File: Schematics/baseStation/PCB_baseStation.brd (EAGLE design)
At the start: 53 x 60 mm, 39 parts, among them U1 ATMEGA328P, U2 MCP1824ST-3302E/DB, Y2 16MHz

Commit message: Base Station PCB improvements
Base_SP 1.1
moved prop plug and ISP closer in
added two resistors to limit voltage from arduino to xbee pin 9(SLP)
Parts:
- added R10: 3.3k, SparkFun-Resistors:0603-RES
- added R9: 1.8k, SparkFun-Resistors:0603-RES
- moved R2 6.48 mm to (17.8, 35.6)
- moved R1 6.48 mm to (17.8, 41.9)
- moved R4 6.48 mm to (17.8, 47.0)
- moved C1 6.35 mm to (29.2, 47.0)
- moved U2 6.35 mm to (22.9, 52.1)
- moved R6 5.08 mm to (27.9, 34.3)
- moved U$1 5.08 mm to (22.9, 30.5)
- moved R3 4.02 mm to (27.9, 24.1)
- moved GND13 3.81 mm to (6.35, 30.5)
- moved RST2 3.81 mm to (6.35, 33.0)
- moved RX1 3.81 mm to (6.35, 35.6)
- moved TX1 3.81 mm to (6.35, 38.1)
- moved 1 3.81 mm to (44.5, 49.5)
- moved 2 3.81 mm to (47.0, 49.5)
- moved 3 3.81 mm to (44.5, 47.0)
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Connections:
- new net N$6: R10.1, R9.2, U$1.9
- new net PD4: R9.1, U1.2
- net GND: now also R10.2
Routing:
- net PD4: track 0.00 -> 27.5 mm, vias 0 -> 2
- net N$6: track 0.00 -> 24.7 mm
- net N$15: track 22.6 -> 12.2 mm, vias 4 -> 0
- net N$19: track 73.3 -> 64.8 mm, vias 1 -> 2
- net DOUT: track 47.6 -> 41.2 mm
- net N$13: track 36.9 -> 42.1 mm, vias 1 -> 2
- net DIN: track 39.7 -> 35.5 mm
- net 4: track 32.5 -> 29.6 mm, vias 0 -> 1
- net N$4: track 3.94 -> 6.08 mm
- net N$10: track 43.1 -> 44.9 mm
- net N$20: track 66.6 -> 65.1 mm
- net 3: track 32.0 -> 30.6 mm, vias 1 -> 0
- net N$14: track 9.40 -> 10.7 mm
- net N$9: track 21.8 -> 20.8 mm
- net N$3: track 16.1 -> 15.1 mm
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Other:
- board text added: "BASE_SP 1.1"
- board text removed: "BASE_SP 1.0"

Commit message: Base Station PCB Improvements
Base_SP 1.3
fixed SIM900 pins that go to Arduino
changed xbee pin that goes to Arduino
created table of base Arduino pins and where they go to
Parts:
- added SM_5V, SM_PWR: M01PTH, SparkFun-Connectors:1X01
- moved R6 19.1 mm to (12.7, 22.9)
- moved PWR 18.2 mm to (18.4, 2.54)
- moved R10 16.6 mm to (17.8, 31.8), turned to 180 degrees
- moved R8 14.0 mm to (36.8, 35.6)
- moved C2 10.5 mm to (16.5, 7.62), turned to 90 degrees
- moved R9 7.41 mm to (17.8, 35.6)
- moved R3 6.84 mm to (30.5, 17.8)
- moved R7 6.48 mm to (12.7, 17.8), turned to 90 degrees
- moved R5 3.81 mm to (49.5, 35.6)
- moved R2 3.81 mm to (17.8, 39.4)
- moved SOLAR 2.54 mm to (25.4, 4.45)
- moved R1 1.27 mm to (17.8, 43.2)
- renumbered GND to SM_GND, RST to SM_RST, RX to SM_RX, TX to SM_TX
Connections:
- new net PB0: SM_TX.1, U1.12
- new net PD2: SM_PWR.1, U1.32
- new net PD3: SM_RST.1, U1.1
- new net PD7: SM_RX.1, U1.11
- net N$19: no longer SM_TX.1
- net N$20: no longer SM_RX.1
- net RST: no longer SM_RST.1
- net VCC: now also SM_5V.1; no longer 5V.1
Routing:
- net VCC: track 144.3 -> 250.7 mm, vias 2 -> 3
- net RST: track 102.7 -> 179.4 mm, vias 2 -> 5
- net N$21: track 0.00 -> 65.1 mm, vias 0 -> 2
- net N$19: track 64.8 -> 122.1 mm, vias 2 -> 3
- net N$10: track 44.9 -> 97.5 mm, vias 1 -> 2
- net PD3: track 0.00 -> 46.3 mm, vias 0 -> 1
- net PD7: track 0.00 -> 44.3 mm, vias 0 -> 1
- net PD2: track 0.00 -> 42.5 mm, vias 0 -> 1
- net PB0: track 0.00 -> 41.6 mm, vias 0 -> 1
- net DOUT: track 41.2 -> 82.6 mm, vias 2 -> 4
- net DIN: track 35.5 -> 73.6 mm, vias 2 -> 4
- net 4: track 29.6 -> 65.2 mm, vias 1 -> 0
- net 1: track 32.8 -> 61.8 mm
- net PD4: track 27.5 -> 55.5 mm, vias 2 -> 0
- net 3: track 30.6 -> 55.2 mm, vias 0 -> 1
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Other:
- board text added: "BASE_SP 1.2"
- board text added: "BASE_SP 1.3"
- board text removed: "BASE_SP 1.1"

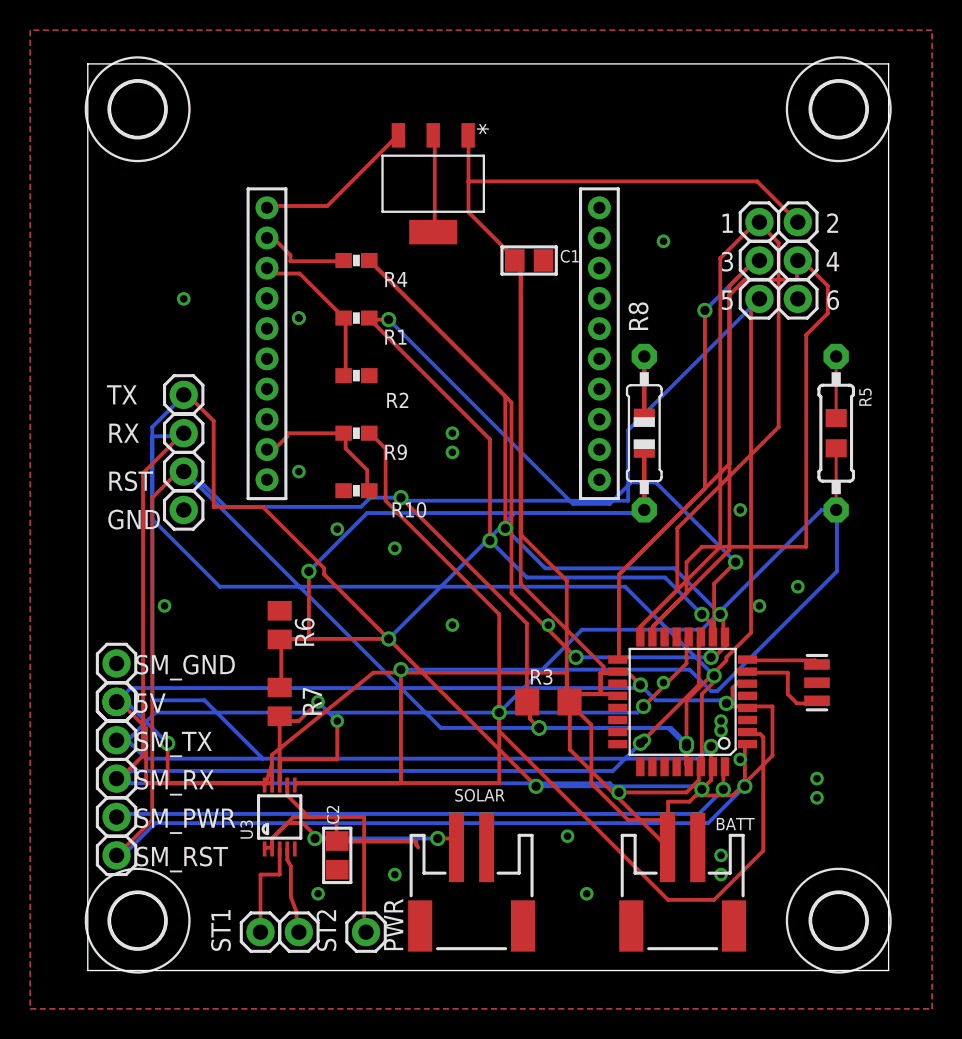
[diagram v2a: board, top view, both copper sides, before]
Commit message: PCB Base Station Improvements
Base_SP 1.4
fixed issues that were occurring with code
fixed SIM900 pins that go to Arduino
changed xbee pin that goes to Arduino
created table of base Arduino pins and where they go to
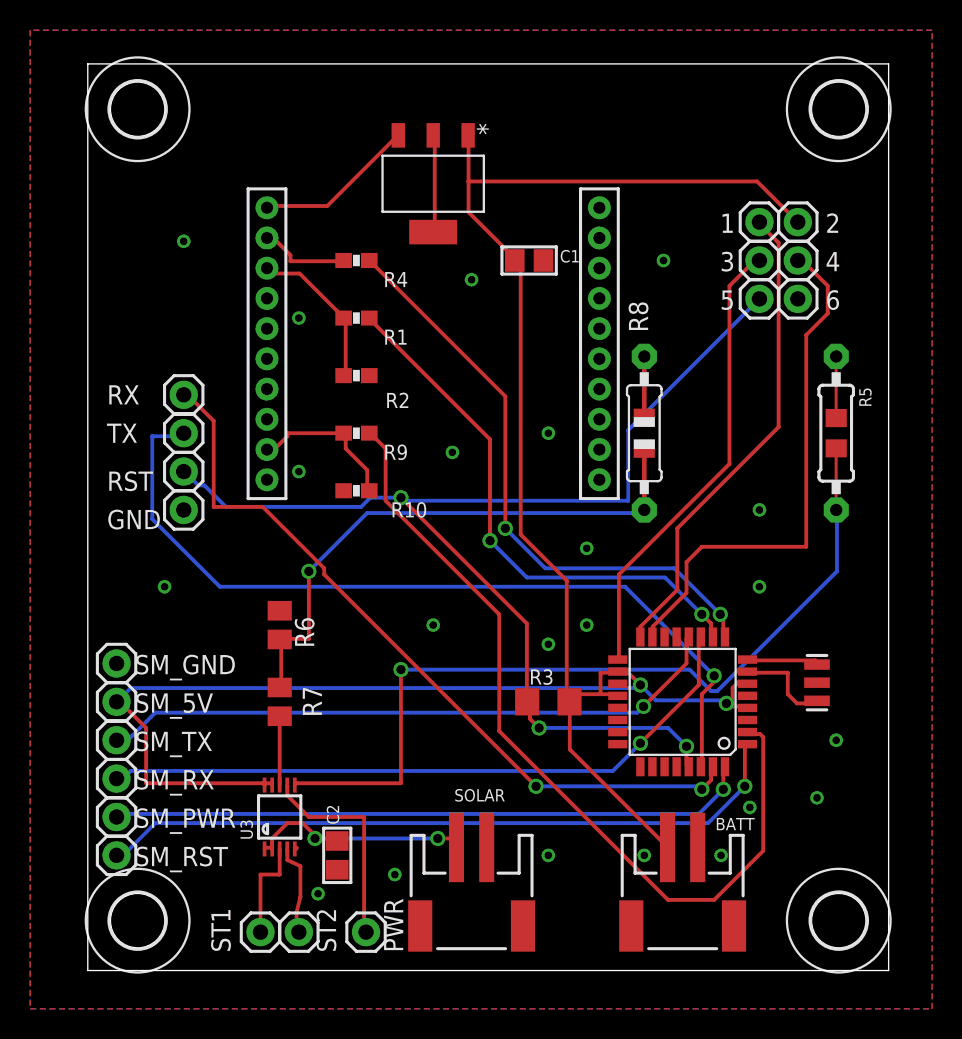
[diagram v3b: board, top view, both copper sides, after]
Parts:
- removed 5V: M01PTH, SparkFun-Connectors:1X01
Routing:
- net VCC: track 250.7 -> 144.0 mm, vias 3 -> 2
- net RST: track 179.4 -> 78.4 mm, vias 5 -> 3
- net N$19: track 122.1 -> 50.6 mm, vias 3 -> 2
- net N$21: track 65.1 -> 0.00 mm, vias 2 -> 0
- net N$10: track 97.5 -> 51.4 mm, vias 2 -> 1
- net DOUT: track 82.6 -> 39.7 mm, vias 4 -> 2
- net DIN: track 73.6 -> 35.9 mm, vias 4 -> 2
- net 4: track 65.2 -> 34.9 mm
- net 1: track 61.8 -> 31.8 mm
- net N$13: track 61.2 -> 33.5 mm, vias 2 -> 1
- net 3: track 55.2 -> 30.6 mm, vias 1 -> 0
- net N$15: track 17.8 -> 4.56 mm, vias 2 -> 0
- net N$9: track 28.8 -> 16.6 mm
- net GND: track 0.00 -> 0.40 mm, vias 27 -> 22
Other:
- board text added: "BASE_SP 1.4"
- board text removed: "BASE_SP 1.2"
- board text removed: "BASE_SP 1.3"

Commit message: Base Station PCB Improvements
Base_SP 1.5
- Fix: connected Regulator for XBee to GND
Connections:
- removed net N$12: U2.2, U2.4
- net GND: now also U2.2, U2.4
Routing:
- net N$12: track 6.54 -> 0.00 mm
- net GND: track 0.40 -> 6.94 mm
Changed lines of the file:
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@@
 <wire x1="48.1584" y1="20.32" x2="48.26" y2="20.25" width="0.254" layer="1"/>
-</signal>
-<signal name="N$12">
-<contactref element="U2" pad="4"/>
-<contactref element="U2" pad="2"/>
-<wire x1="22.9616" y1="48.9712" x2="22.9616" y2="55.2704" width="0.254" layer="1"/>
-<wire x1="22.9616" y1="55.2704" x2="22.86" y2="55.2704" width="0.254" layer="1"/>
-<wire x1="22.9616" y1="48.9712" x2="22.86" y2="48.8696" width="0.254" layer="1"/>
 </signal>
 <signal name="N$14">
@@
 <via x="38.1" y="46.99" extent="1-16" drill="0.5"/>
 <via x="44.45" y="30.48" extent="1-16" drill="0.5"/>
+<contactref element="U2" pad="4"/>
+<contactref element="U2" pad="2"/>
+<wire x1="22.9616" y1="48.9712" x2="22.9616" y2="55.2704" width="0.254" layer="1"/>
+<wire x1="22.9616" y1="55.2704" x2="22.86" y2="55.2704" width="0.254" layer="1"/>
+<wire x1="22.9616" y1="48.9712" x2="22.86" y2="48.8696" width="0.254" layer="1"/>
 </signal>
 <signal name="VCC">
